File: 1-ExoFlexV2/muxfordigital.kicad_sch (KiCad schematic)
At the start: 18 parts, among them U104 AND Gate, U105 AND Gate, U106 AND Gate, U107 Inverter, U108 Inverter, U109 AND Gate, U110 Inverter, U111 Inverter, U112 Inverter, U113 Inverter, U114 MUX 8:1, U115 MUX 8:1, U116 MUX 8:1, U117 MUX 8:1, U118 OR Gate, U119 OR Gate, U120 OR Gate

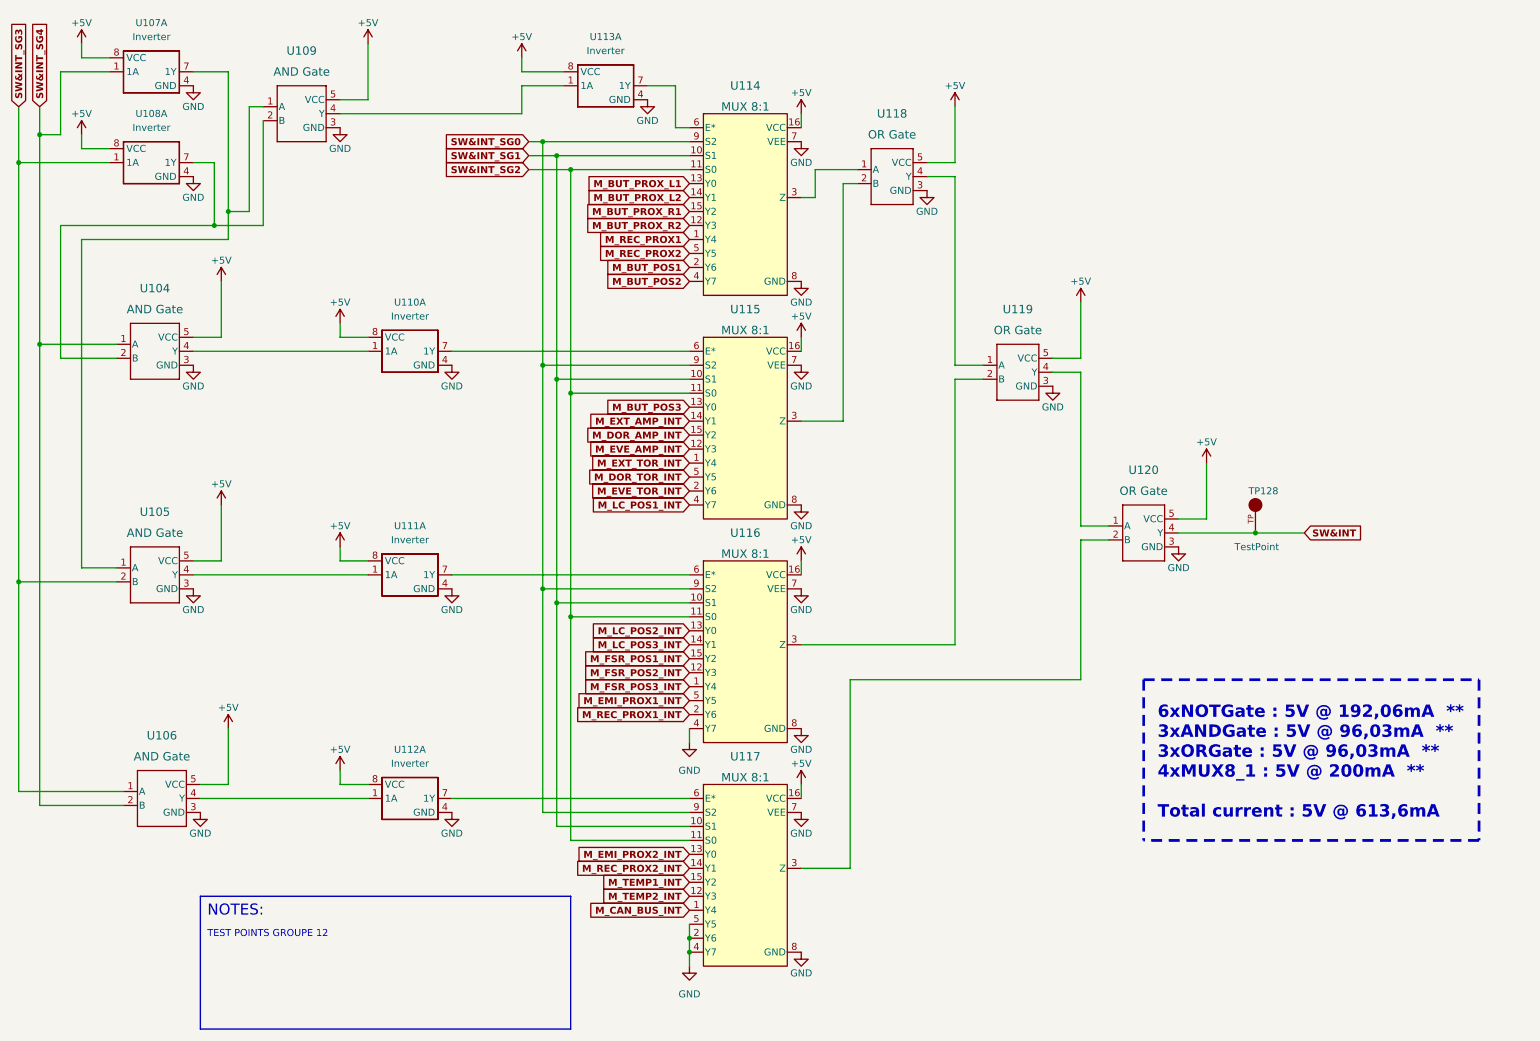
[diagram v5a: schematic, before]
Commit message: Finalisation schéma FIN
- Changement des uméro pour les inverseurs
- Changement des connecteur et début de placement
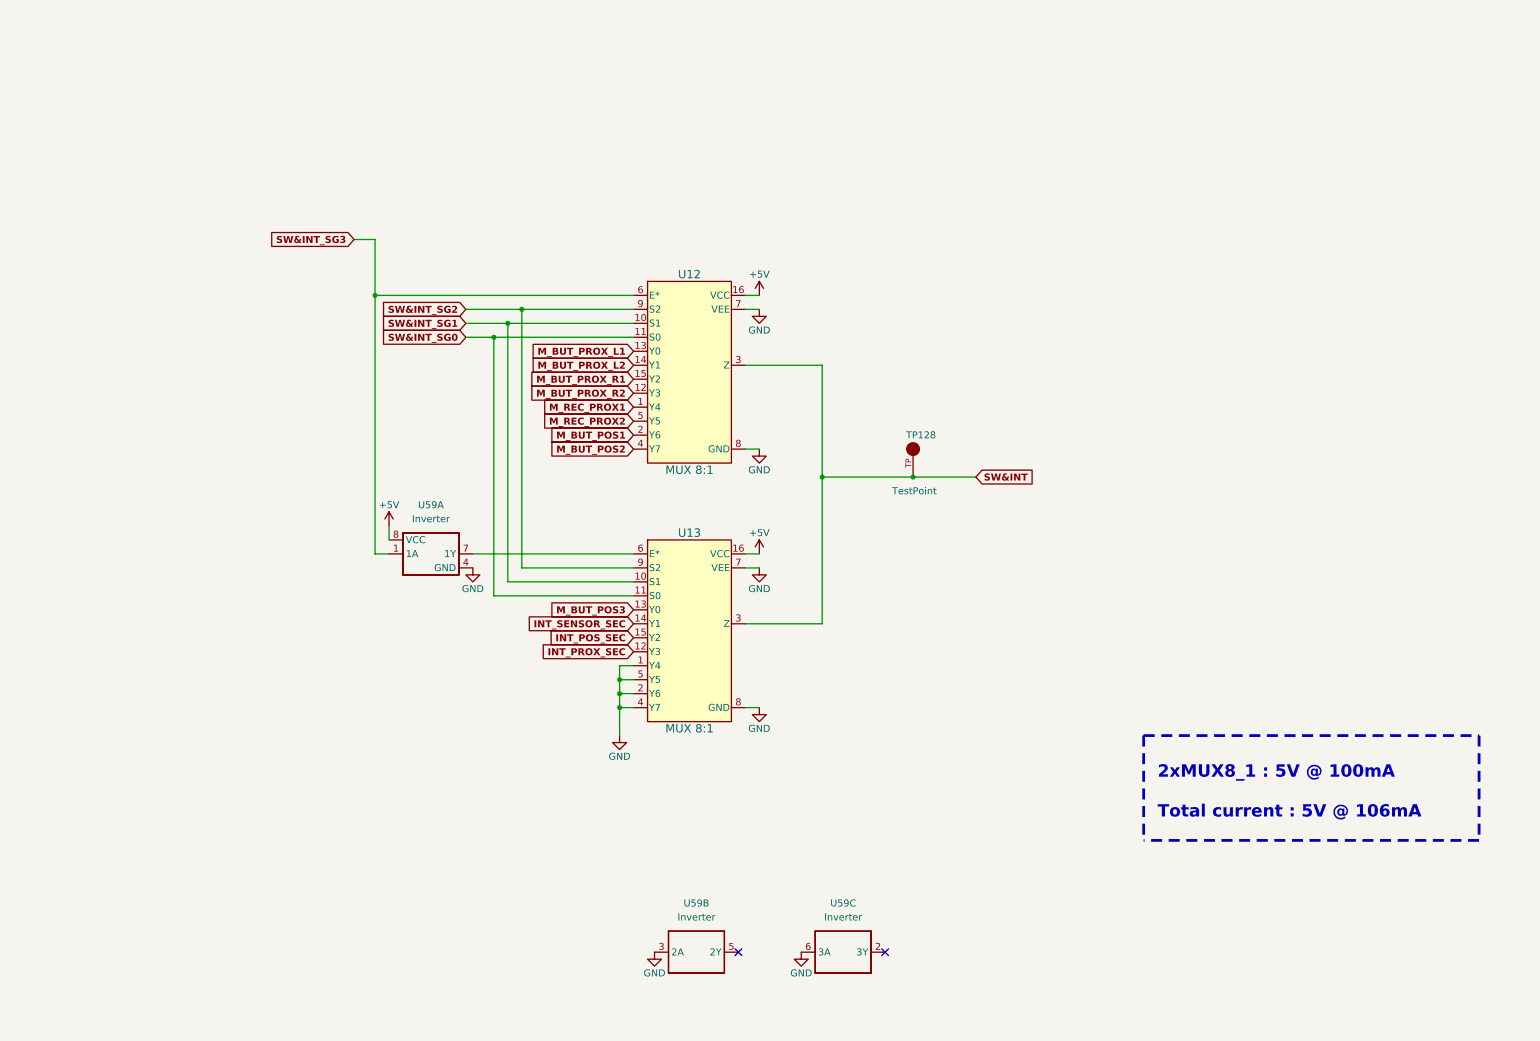
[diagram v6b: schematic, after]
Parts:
- removed U104, U105, U106, U109: AND Gate, FootPrint:SOT95P270X145-5N, symbol SymLib:SN74LVC1G08DBVR
- removed U107, U108, U110, U111, U112, U113: Inverter, FootPrint:SN74LVC3G14DCUT, symbol SymLib:SN74LVC3G14DCUT_V2
- removed U114, U115, U116, U117: MUX 8:1, FootPrint:SOT403-1_NXP, symbol SymLib:74HC4051PW
- removed U118, U119, U120: OR Gate, FootPrint:SOT95P270X145-5N, symbol SymLib:SN74LVC1G32DBVR
- added U12, U13: MUX 8:1, FootPrint:SOT403-1_NXP, symbol SymLib:74HC4051PW
- added U59: Inverter, FootPrint:SN74LVC3G14DCUT, symbol SymLib:SN74LVC3G14DCUT_V2
- TP128: NOTES (none) -> DO NOT POPULATE; PURCHASE-URL https://pricing.snapeda.com/search/part/5005/?ref=eda -> (none)
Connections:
- net +5V: now also U12.16 (VCC), U13.16 (VCC), U59.8 (VCC)
- net GND: now also U12.7 (VEE), U12.8 (GND), U13.1 (Y4), U13.2 (Y6), U13.4 (Y7), U13.5 (Y5), U13.7 (VEE), U13.8 (GND), U59.3 (2A), U59.4 (GND), U59.6 (3A)
- net M_BUT_POS1: now also U12.2 (Y6)
- net M_BUT_POS2: now also U12.4 (Y7)
- net M_BUT_POS3: now also U13.13 (Y0)
- net M_BUT_PROX_L1: now also U12.13 (Y0)
- net M_BUT_PROX_L2: now also U12.14 (Y1)
- net M_BUT_PROX_R1: now also U12.15 (Y2)
- net M_BUT_PROX_R2: now also U12.12 (Y3)
- net M_REC_PROX1: now also U12.1 (Y4)
- net M_REC_PROX2: now also U12.5 (Y5)
- net SW&INT: now also U12.3 (Z), U13.3 (Z)
- net SW&INT_SG0: now also U12.11 (S0), U13.11 (S0)
- net SW&INT_SG1: now also U12.10 (S1), U13.10 (S1)
- net SW&INT_SG2: now also U12.9 (S2), U13.9 (S2)
- net SW&INT_SG3: now also U12.6 (E*), U59.1 (1A)
- new net: U13.6 (E*), U59.7 (1Y)
- new net INT_POS_SEC: U13.15 (Y2)
- new net INT_PROX_SEC: U13.12 (Y3)
- new net INT_SENSOR_SEC: U13.14 (Y1)
- no-connect marks 0 -> 2
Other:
- note added: "2xMUX8_1 : 5V @ 100mA Total current : 5V @ 106mA"
- note removed: "6xNOTGate : 5V @ 192,06mA ** 3xANDGate : 5V @ 96,03mA ** 3xORGate : 5V @ 96,03mA ** 4xMUX8_1 : 5V @ 200mA ** Total current : 5V @ 613,6mA"
- note removed: "NOTES:"
- note removed: "TEST POINTS GROUPE 12"
- moved on the sheet: TP128
